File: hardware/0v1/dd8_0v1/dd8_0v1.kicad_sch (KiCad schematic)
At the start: 5 parts, among them U1 W65C02SxP, U2 AS7C164A, U3 AT28C64B, U4 DEM16101

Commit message: dd8 v0.1 updated
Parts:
- removed U4: DEM16101, Display:LCD-016N002L, symbol Display_Character:LCD-016N002L
- removed U5: ~, symbol dd8_components_library:4x4_Keypad
- added U4: keypad_ctrl, symbol dd8_components_library:keypad_ctrl
- added U5: 4x4 keypad, symbol dd8_components_library:4x4_keypad
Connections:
- net +5V: now also U4. (~{WE})
- net A0: now also U4. (~{WE})
- net A1: now also U4. (~{WE})
- net D0: now also U4. (~{WE})
- net D1: now also U4. (~{WE})
- net D2: now also U4. (~{WE})
- net D3: now also U4. (~{WE})
- net D4: now also U4. (~{WE})
- net D5: now also U4. (~{WE})
- net D6: now also U4. (~{WE})
- net D7: now also U4. (~{WE})
- net GND: now also U4. (~{WE})
- new net: U4. (~{WE}), U5.1 (C1)
- new net: U4. (~{WE}), U5.2 (C2)
- new net: U4. (~{WE}), U5.3 (C3)
- new net: U4. (~{WE}), U5.4 (C4)
- new net: U4. (~{WE}), U5.5 (R1)
- new net: U4. (~{WE}), U5.6 (R2)
- new net: U4. (~{WE}), U5.7 (R3)
- new net: U4. (~{WE}), U5.8 (R4)

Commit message: Updates
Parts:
- removed U4: keypad_ctrl, symbol dd8_components_library:keypad_ctrl
- added DS1: LCD 20x4, Display:WC1602A, symbol Display_Character:WC1602A
- added R1: 220, symbol Device:R
- added RV1: 10k, symbol Device:R_Potentiometer_Trim
- added U6: ~, symbol dd8_components_library:keypad_ctrl
- added U7: ~, symbol dd8_components_library:ics_v0
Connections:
- net +5V: now also U3.27 (~{WE}), DS1.2 (VDD), R1.2, RV1.3, U6. (VSS), U6.6 (~{WE}), U7. (VSS)
- net A0: now also DS1.4 (RS), U6.1 (A0)
- net A1: now also U6.2 (A1)
- net A13: now also U7.4 (A13)
- net A14: now also U7.5 (A14)
- net A15: now also U7.6 (A15)
- net D0: now also DS1.7 (D0), U6.11 (D0)
- net D1: now also DS1.8 (D1), U6.12 (D1)
- net D2: now also DS1.9 (D2), U6.16 (D2)
- net D3: now also DS1.10 (D3), U6.17 (D3)
- net D4: now also DS1.11 (D4), U6.18 (D4)
- net D5: now also DS1.12 (D5), U6.19 (D5)
- net D6: now also DS1.13 (D6), U6.20 (D6)
- net D7: now also DS1.14 (D7), U6.21 (D7)
- net GND: now also DS1.1 (VSS), DS1.16 (LED(-)), RV1.1, U6. (VSS), U7. (VSS)
- net at U5.1 (C1): now also U6.24 (C0)
- net at U5.2 (C2): now also U6.25 (C1)
- net at U5.3 (C3): now also U6.26 (C2)
- net at U5.4 (C4): now also U6.27 (C3)
- net at U5.5 (R1): now also U6.28 (R0)
- net at U5.6 (R2): now also U6.29 (R1)
- net at U5.7 (R3): now also U6.33 (R2)
- net at U5.8 (R4): now also U6.34 (R3)
- net R~{W}: now reaches U1.34 (R/~{W})
- net R~{W}: now also DS1.5 (R/W), U7.1 (R~{W})
- net PHI2: now reaches U1.39 (ϕ2)
- net PHI2: now also U7.2 (CLK)
- net ~{CE_ROM}: now reaches U3.20 (~{CE})
- net ~{CE_ROM}: now also U7.29 (~{CE_{ROM}})
- net ~{OE}: now reaches U3.22 (~{OE})
- net ~{OE}: now also U2.22 (~{OE}), U6.5 (~{OE}), U7.24 (~{OE})
- net ~{CE_RAM}: now reaches U2.20 (~{CE})
- net ~{CE_RAM}: now also U7.28 (~{CE_{RAM}})
- net ~{WE}: now reaches U2.27 (~{WE})
- net ~{WE}: now also U7.25 (~{WE})
- new net: DS1.15 (LED(+)), R1.1
- new net: DS1.3 (VO), RV1.2
- new net E_LCD: DS1.6 (E), U7.26 (E_{LCD})
- new net ~{CE_KPAD}: U6.4 (~{CE}), U7.27 (~{CE_{KYPAD}})
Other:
- moved on the sheet: U1, U2, U3, U5

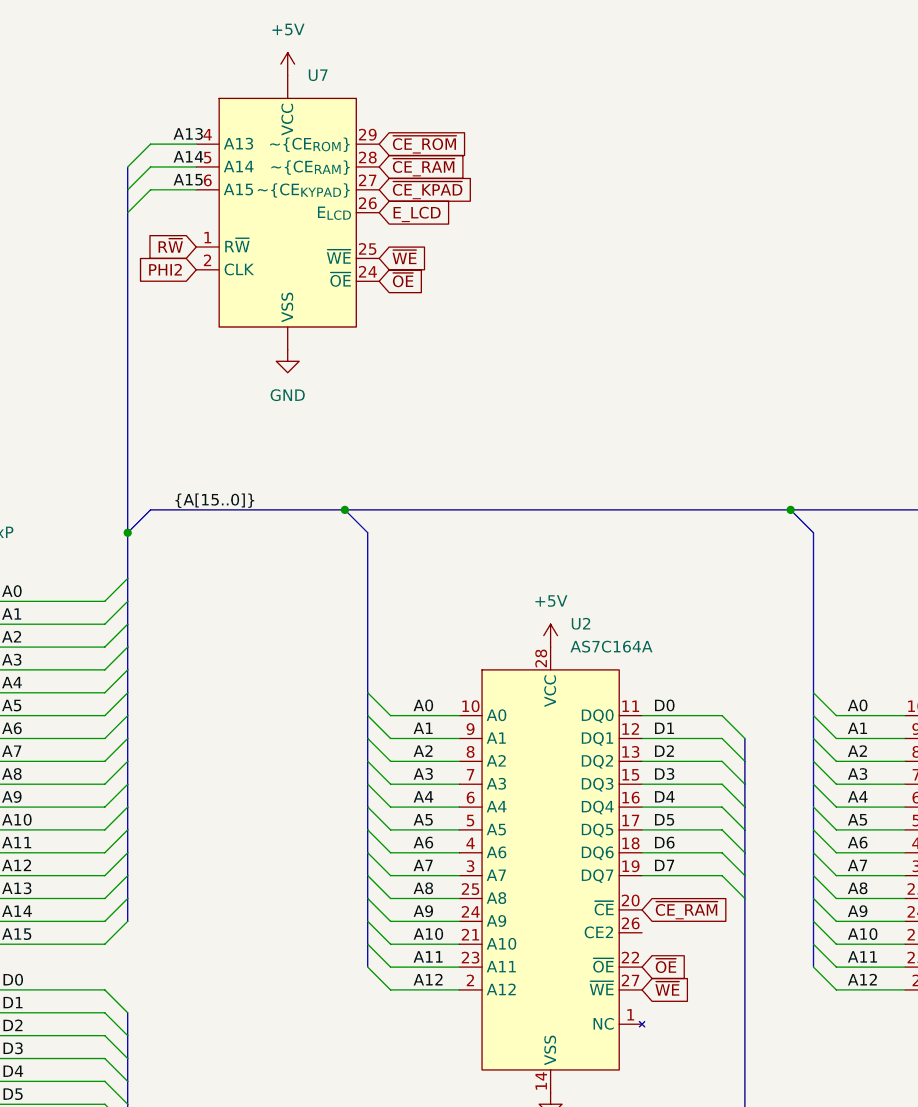
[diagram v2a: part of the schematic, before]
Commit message: Arduino ROM emulator
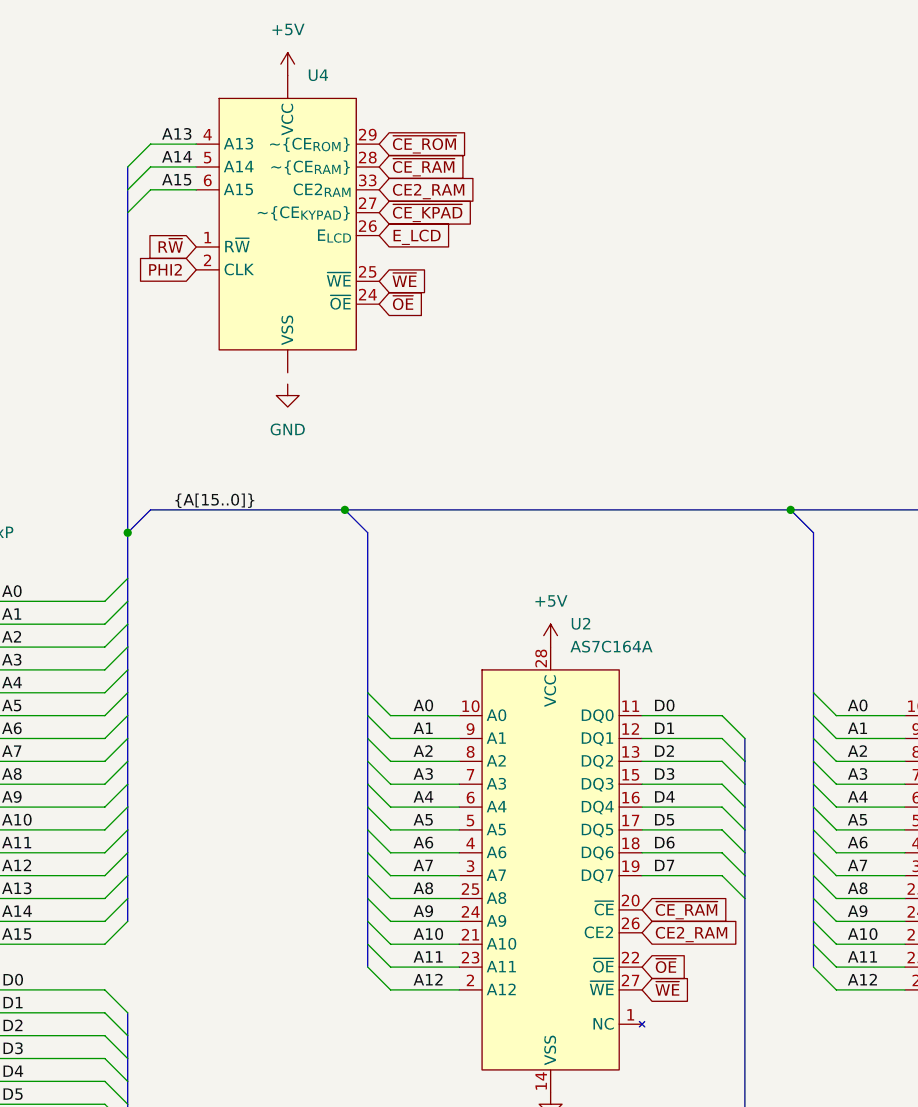
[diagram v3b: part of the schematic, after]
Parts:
- removed U7: ~, symbol dd8_components_library:ics_v0
- added U4: ~, symbol dd8_components_library:ics_v0
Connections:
- net +5V: now also U4. (VSS)
- net A13: now also U4.4 (A13)
- net A14: now also U4.5 (A14)
- net A15: now also U4.6 (A15)
- net E_LCD: now also U4.26 (E_{LCD})
- net PHI2: now also U4.2 (CLK)
- net R~{W}: now also U4.1 (R~{W})
- net ~{CE_KPAD}: now also U4.27 (~{CE_{KYPAD}})
- net ~{CE_RAM}: now also U4.28 (~{CE_{RAM}})
- net ~{CE_ROM}: now also U4.29 (~{CE_{ROM}})
- net ~{OE}: now also U4.24 (~{OE})
- net ~{WE}: now also U4.25 (~{WE})
- net CE2_RAM: now reaches U2.26 (CE2)
- net CE2_RAM: now also U4.33 (CE2_{RAM})
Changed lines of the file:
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@@
     (effects (font (size 1.27 1.27)) (justify left bottom))
   )
-  (label "A15" (at 97.79 54.61 0) (fields_autoplaced)
+  (label "A15" (at 96.52 54.61 0) (fields_autoplaced)
     (effects (font (size 1.27 1.27)) (justify left bottom))
   )
@@
     (effects (font (size 1.27 1.27)) (justify left bottom))
   )
-  (label "A13" (at 97.79 49.53 0) (fields_autoplaced)
+  (label "A13" (at 96.52 49.53 0) (fields_autoplaced)
     (effects (font (size 1.27 1.27)) (justify left bottom))
   )
@@
     (effects (font (size 1.27 1.27)) (justify left bottom))
   )
-  (label "A14" (at 97.79 52.07 0) (fields_autoplaced)
+  (label "A14" (at 96.52 52.07 0) (fields_autoplaced)
     (effects (font (size 1.27 1.27)) (justify left bottom))
   )
@@
     )
   )
-  (global_label "E_LCD" (shape input) (at 120.65 57.15 0) (fields_autoplaced)
-    (effects (font (size 1.27 1.27)) (justify left))
-    (property "Intersheetrefs" "${INTERSHEET_REFS}" (at 129.3199 57.15 0)
-      (effects (font (size 1.27 1.27)) (justify left) hide)
-    )
-  )
-  (global_label "~{CE_KPAD}" (shape input) (at 120.65 54.61 0) (fields_autoplaced)
-    (effects (font (size 1.27 1.27)) (justify left))
-    (property "Intersheetrefs" "${INTERSHEET_REFS}" (at 131.9204 54.61 0)
+  (global_label "E_LCD" (shape input) (at 120.65 59.69 0) (fields_autoplaced)
+    (effects (font (size 1.27 1.27)) (justify left))
+    (property "Intersheetrefs" "${INTERSHEET_REFS}" (at 129.3199 59.69 0)
+      (effects (font (size 1.27 1.27)) (justify left) hide)
+    )
+  )
+  (global_label "~{CE_KPAD}" (shape input) (at 120.65 57.15 0) (fields_autoplaced)
+    (effects (font (size 1.27 1.27)) (justify left))
+    (property "Intersheetrefs" "${INTERSHEET_REFS}" (at 131.9204 57.15 0)
       (effects (font (size 1.27 1.27)) (justify left) hide)
     )
@@
     )
   )
+  (global_label "CE2_RAM" (shape input) (at 149.86 137.16 0) (fields_autoplaced)
+    (effects (font (size 1.27 1.27)) (justify left))
+    (property "Intersheetrefs" "${INTERSHEET_REFS}" (at 161.2513 137.16 0)
+      (effects (font (size 1.27 1.27)) (justify left) hide)
+    )
+  )
   (global_label "~{CE_RAM}" (shape input) (at 120.65 52.07 0) (fields_autoplaced)
     (effects (font (size 1.27 1.27)) (justify left))
@@
     )
   )
-  (global_label "~{OE}" (shape input) (at 120.65 64.77 0) (fields_autoplaced)
-    (effects (font (size 1.27 1.27)) (justify left))
-    (property "Intersheetrefs" "${INTERSHEET_REFS}" (at 126.1147 64.77 0)
+  (global_label "~{OE}" (shape input) (at 120.65 67.31 0) (fields_autoplaced)
+    (effects (font (size 1.27 1.27)) (justify left))
+    (property "Intersheetrefs" "${INTERSHEET_REFS}" (at 126.1147 67.31 0)
       (effects (font (size 1.27 1.27)) (justify left) hide)
     )
@@
     )
   )
+  (global_label "CE2_RAM" (shape input) (at 120.65 54.61 0) (fields_autoplaced)
+    (effects (font (size 1.27 1.27)) (justify left))
+    (property "Intersheetrefs" "${INTERSHEET_REFS}" (at 132.0413 54.61 0)
+      (effects (font (size 1.27 1.27)) (justify left) hide)
+    )
+  )
   (global_label "~{CE_ROM}" (shape input) (at 199.39 134.62 0) (fields_autoplaced)
     (effects (font (size 1.27 1.27)) (justify left))
@@
     )
   )
-  (global_label "~{WE}" (shape input) (at 120.65 62.23 0) (fields_autoplaced)
-    (effects (font (size 1.27 1.27)) (justify left))
-    (property "Intersheetrefs" "${INTERSHEET_REFS}" (at 126.2356 62.23 0)
+  (global_label "~{WE}" (shape input) (at 120.65 64.77 0) (fields_autoplaced)
+    (effects (font (size 1.27 1.27)) (justify left))
+    (property "Intersheetrefs" "${INTERSHEET_REFS}" (at 126.2356 64.77 0)
       (effects (font (size 1.27 1.27)) (justify left) hide)
     )
@@
         (path "/dbac5f98-a792-480e-9737-70995185953b"
           (reference "#PWR06") (unit 1)
-        )
-      )
-    )
-  )
-  (symbol (lib_name "ics_v0_1") (lib_id "dd8_components_library:ics_v0") (at 110.49 57.15 0) (unit 1)
-    (in_bom yes) (on_board yes) (dnp no) (fields_autoplaced)
-    (property "Reference" "U7" (at 112.6841 41.91 0)
-      (effects (font (size 1.27 1.27)) (justify left))
-    )
-    (property "Value" "~" (at 110.49 45.085 0)
-      (effects (font (size 1.27 1.27)))
-    )
-    (property "Footprint" "" (at 110.49 45.085 0)
-      (effects (font (size 1.27 1.27)) hide)
-    )
-    (property "Datasheet" "" (at 110.49 45.085 0)
-      (effects (font (size 1.27 1.27)) hide)
-    )
-    (pin "6")
-    (pin "27")
-    (pin "5")
-    (pin "25")
-    (pin "4")
-    (pin "28")
-    (pin "1")
-    (pin "")
-    (pin "")
-    (pin "26")
-    (pin "29")
-    (pin "2")
-    (pin "24")
-    (instances
-      (project "dd8_0v1"
-        (path "/dbac5f98-a792-480e-9737-70995185953b"
-          (reference "U7") (unit 1)
         )
       )
@@
     )
   )
+  (symbol (lib_id "dd8_components_library:ics_v0") (at 110.49 57.15 0) (unit 1)
+    (in_bom yes) (on_board yes) (dnp no) (fields_autoplaced)
+    (property "Reference" "U4" (at 112.6841 41.91 0)
+      (effects (font (size 1.27 1.27)) (justify left))
+    )
+    (property "Value" "~" (at 110.49 45.085 0)
+      (effects (font (size 1.27 1.27)))
+    )
+    (property "Footprint" "" (at 110.49 45.085 0)
+      (effects (font (size 1.27 1.27)) hide)
+    )
+    (property "Datasheet" "" (at 110.49 45.085 0)
+      (effects (font (size 1.27 1.27)) hide)
+    )
+    (pin "2")
+    (pin "29")
+    (pin "25")
+    (pin "6")
+    (pin "")
+    (pin "1")
+    (pin "")
+    (pin "27")
+    (pin "5")
+    (pin "28")
+    (pin "26")
+    (pin "4")
+    (pin "33")
+    (pin "24")
+    (instances
+      (project "dd8_0v1"
+        (path "/dbac5f98-a792-480e-9737-70995185953b"
+          (reference "U4") (unit 1)
+        )
+      )
+    )
+  )
   (symbol (lib_id "power:+5V") (at 207.01 139.7 0) (unit 1)
     (in_bom yes) (on_board yes) (dnp no)
@@
     )
   )
-  (symbol (lib_id "power:GND") (at 110.49 72.39 0) (unit 1)
-    (in_bom yes) (on_board yes) (dnp no) (fields_autoplaced)
-    (property "Reference" "#PWR012" (at 110.49 78.74 0)
-      (effects (font (size 1.27 1.27)) hide)
-    )
-    (property "Value" "GND" (at 110.49 77.47 0)
-      (effects (font (size 1.27 1.27)))
-    )
-    (property "Footprint" "" (at 110.49 72.39 0)
-      (effects (font (size 1.27 1.27)) hide)
-    )
-    (property "Datasheet" "" (at 110.49 72.39 0)
-      (effects (font (size 1.27 1.27)) hide)
-    )
+  (symbol (lib_id "power:GND") (at 110.49 76.2 0) (unit 1)
+    (in_bom yes) (on_board yes) (dnp no) (fields_autoplaced)
+    (property "Reference" "#PWR012" (at 110.49 82.55 0)
+      (effects (font (size 1.27 1.27)) hide)
+    )
+    (property "Value" "GND" (at 110.49 81.28 0)
+      (effects (font (size 1.27 1.27)))
+    )
+    (property "Footprint" "" (at 110.49 76.2 0)
+      (effects (font (size 1.27 1.27)) hide)
+    )
+    (property "Datasheet" "" (at 110.49 76.2 0)
+      (effects (font (size 1.27 1.27)) hide)
+    )

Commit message: Spelling
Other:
- note added: "Bare minium 6502 pc (dd8 v0.1)"
- note removed: "Bear minium 6502 pc (dd8 v0.1)"
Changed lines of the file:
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@@
     (effects (font (size 1.27 1.27)) (justify left bottom))
   )
-  (text "Bear minium 6502 pc (dd8 v0.1) " (at 309.88 278.13 0)
+  (text "Bare minium 6502 pc (dd8 v0.1) " (at 309.88 278.13 0)
     (effects (font (size 1.27 1.27)) (justify left bottom))
   )
